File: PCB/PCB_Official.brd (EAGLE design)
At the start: 100 x 100 mm, 106 parts, among them IC1 MCP73871, J3 455-1750-1-ND, Q1 220mA/50V/3.5Ω, U1 TPS63070, U2 STM32F767ZIT6, U3 STM32L053C8T6, U4 TPS63070, U5 BATTERY-MANAGEMENT-TEMP_BQ274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

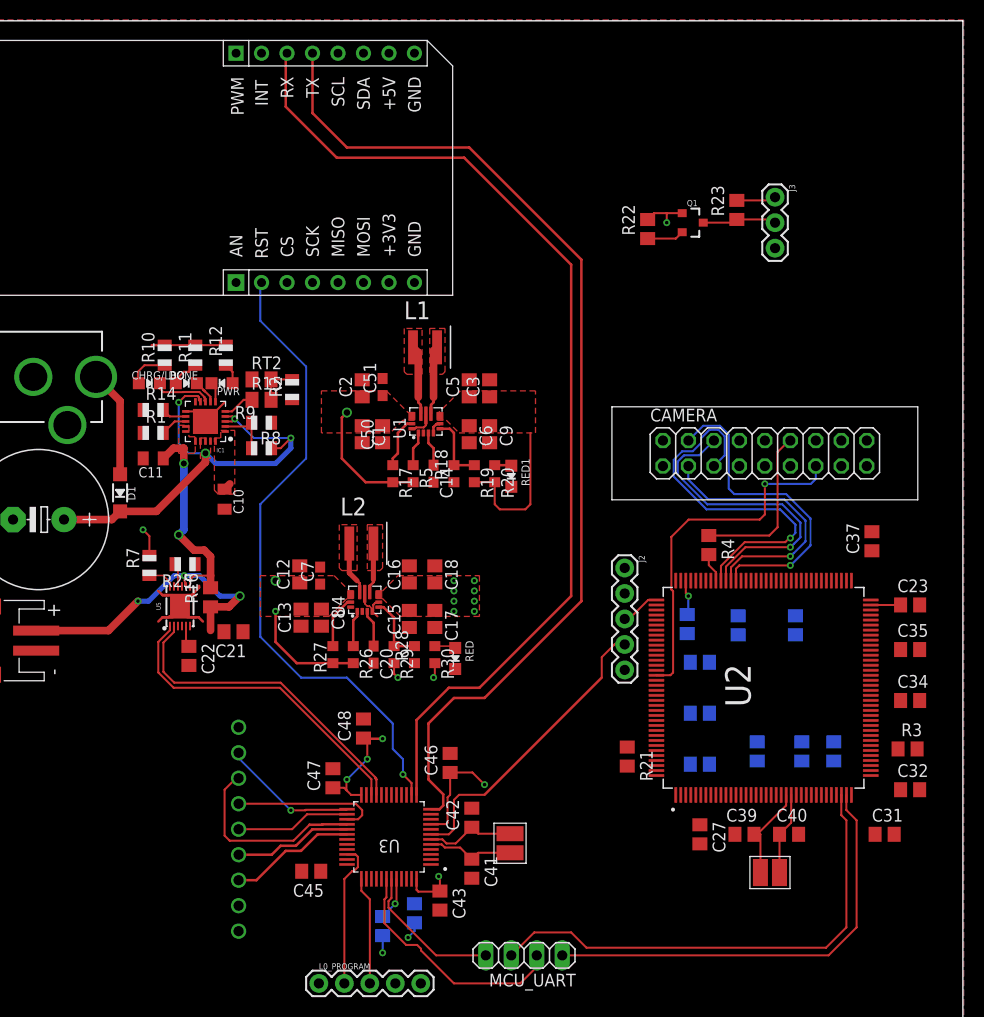
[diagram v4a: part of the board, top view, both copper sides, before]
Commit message: Added PCB pin assignments and routed camera connector.
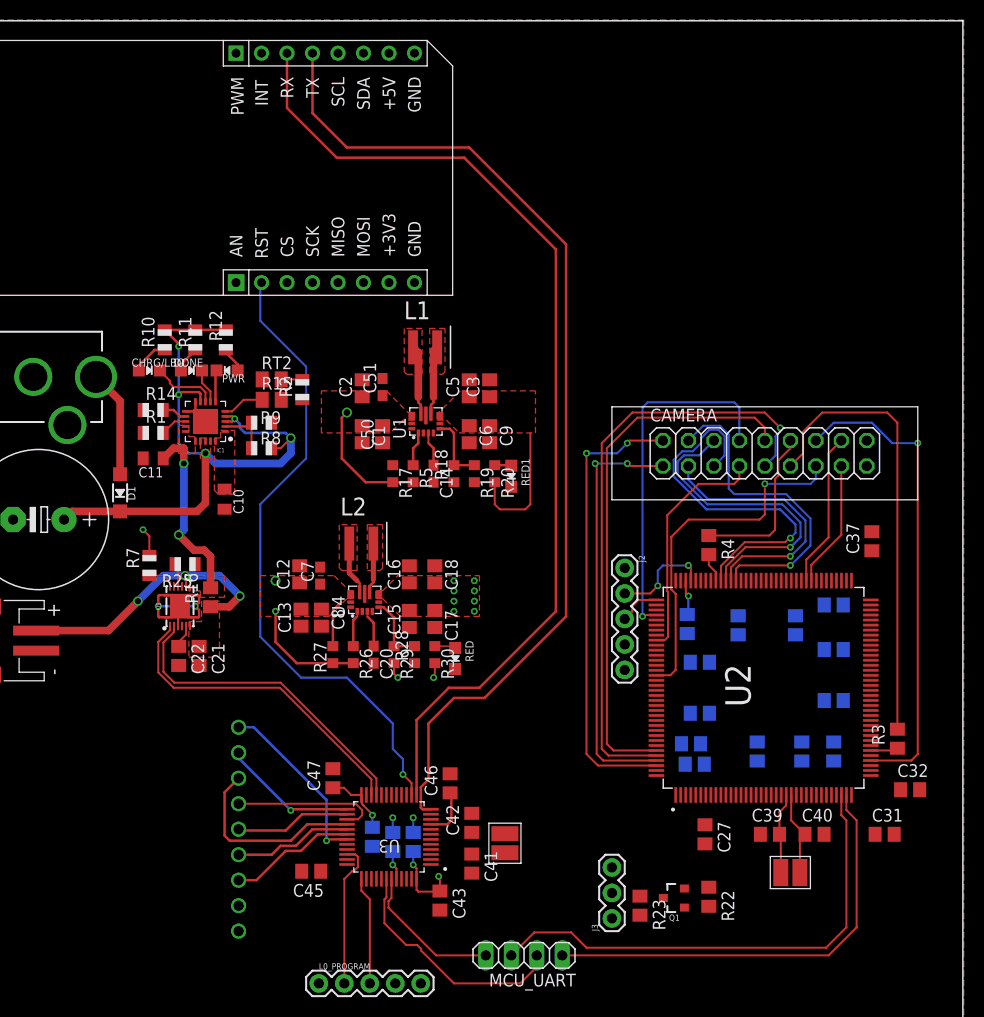
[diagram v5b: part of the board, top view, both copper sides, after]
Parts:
- moved J3 73.7 mm to (65.0, 10.5), turned to 90 degrees
- moved R23 70.0 mm to (67.8, 11.8), turned to 270 degrees
- moved Q1 67.3 mm to (71.2, 12.6), turned to 90 degrees
- moved R22 66.8 mm to (74.7, 12.7), turned to 270 degrees
- moved C48 10.8 mm to (41.1, 18.7), flipped to the bottom, turned to 270 degrees
- moved R24 8.44 mm to (43.2, 18.2), turned to 270 degrees
- moved C23 7.62 mm to (87.1, 41.8), flipped to the bottom
- moved C34 7.62 mm to (87.1, 32.3), flipped to the bottom
- moved C35 7.62 mm to (87.1, 37.3), flipped to the bottom
- moved C44 7.11 mm to (45.2, 18.2), turned to 90 degrees
- moved R21 6.48 mm to (72.9, 27.9), flipped to the bottom, turned to 180 degrees
- moved C21 4.19 mm to (23.9, 36.7), turned to 270 degrees
- moved C39 2.54 mm to (80.8, 18.9)
- moved C40 2.54 mm to (85.2, 18.9)
- moved C46 2.03 mm to (48.9, 24.0)
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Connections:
- removed net TIM3_CH2: Q1.2, R22.1, U2.135
- new net SERVO_PWM: Q1.2, R22.1, U2.18
- net CAM_PWDN: now also U2.142
- net CAM_RET: now also U2.141
- net LORA_RST: now also U3.31
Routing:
- net DCMI_D7: track 0.00 -> 60.3 mm, vias 0 -> 1
- net DCMI_D6: track 0.00 -> 53.4 mm
- net DCMI_HSYNC: track 0.00 -> 47.7 mm, vias 0 -> 1
- net CAM_PWDN: track 0.00 -> 45.6 mm, vias 0 -> 2
- net N$33: track 0.00 -> 45.1 mm
- net CAM_RET: track 0.00 -> 42.1 mm, vias 0 -> 2
- net DCMI_D4: track 0.00 -> 35.6 mm, vias 0 -> 1
- net MCU_RST: track 30.1 -> 0.00 mm
- net DCMI_D5: track 0.00 -> 23.4 mm
- net LORA_RST: track 0.00 -> 17.9 mm, vias 0 -> 1
- net CAM_SDA: track 0.00 -> 15.4 mm
- net CAM_SCL: track 0.00 -> 12.7 mm
- net +3V3: track 37.7 -> 25.7 mm, vias 17 -> 14
- net SYS_JTMS_SWDIO: track 0.00 -> 10.0 mm, vias 0 -> 2
- net VCC: track 56.1 -> 65.9 mm, vias 4 -> 5
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- added copper zone on layer 1, net N$22

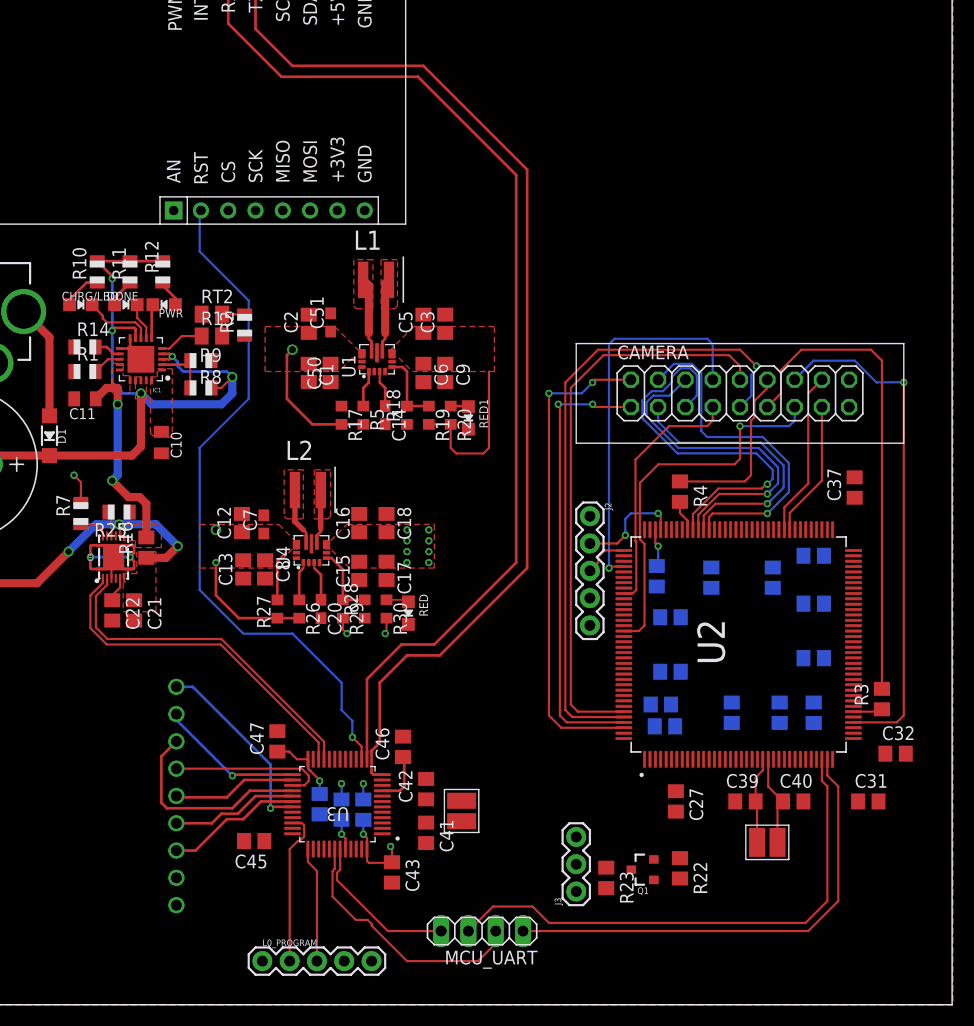
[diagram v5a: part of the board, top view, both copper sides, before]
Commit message: Corrected layout of 5V regulator, WIP for 3.3V regulator. Improved microcontroller layouts as well.
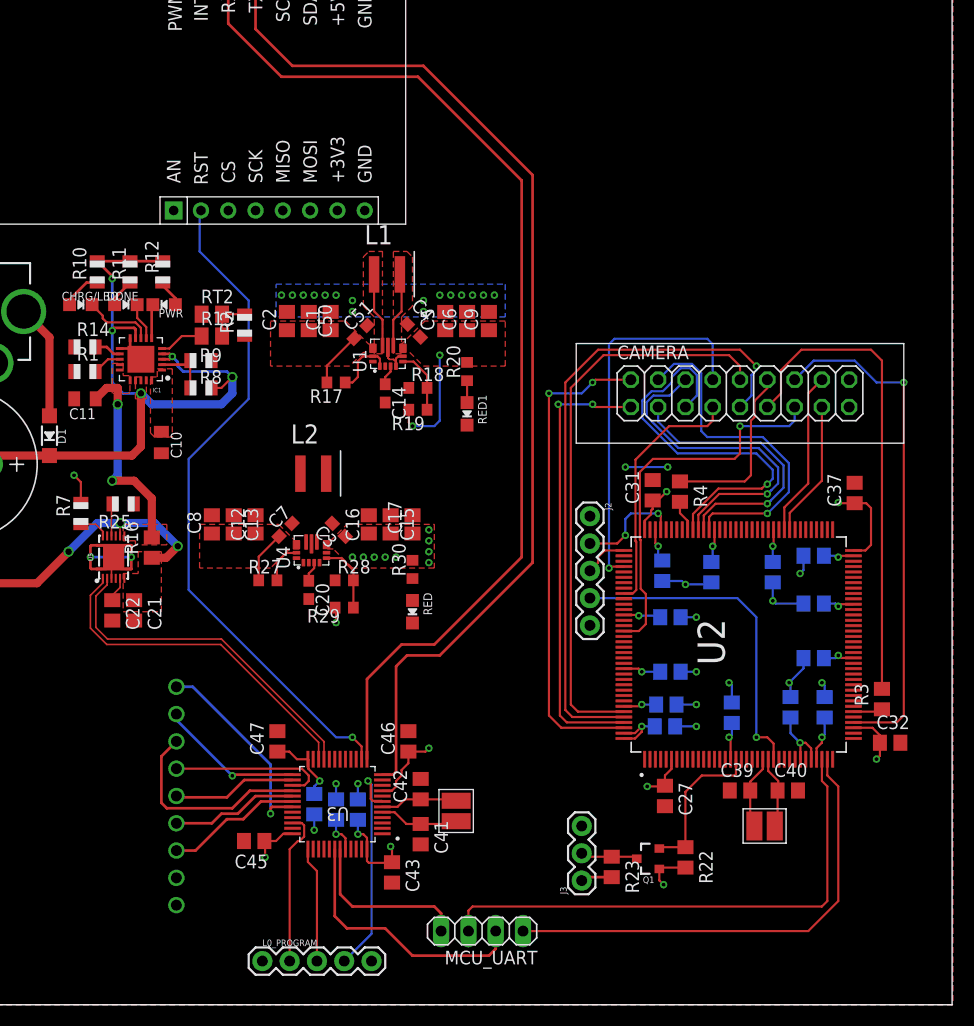
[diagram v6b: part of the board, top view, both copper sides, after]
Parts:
- removed C18: 10uF, adafruit:C0805
- removed R26, R5: 10k, rcl:R0603
- added C4: 10uF, rcl:C0603
- C13, C2: value 10uF -> 0.1uF
- C3: device adafruit:C0805 -> rcl:C0603
- C51, C7: value 0.1uF -> 10uF
- R18: value 68.1k -> 130k
- R19: value 365k -> 680k
- moved C31 35.2 mm to (72.1, 47.9), turned to 90 degrees
- moved C3 21.6 mm to (42.9, 44.2), turned to 135 degrees
- moved C8 6.49 mm to (31.1, 44.7), turned to 90 degrees
- moved C6 6.31 mm to (54.9, 63.6), turned to 90 degrees
- moved C9 6.31 mm to (56.9, 63.6), turned to 90 degrees
- moved C1 5.24 mm to (42.2, 63.6), turned to 90 degrees
- moved C50 5.24 mm to (40.1, 63.6), turned to 90 degrees
- moved C15 5.21 mm to (47.8, 44.7), turned to 90 degrees
- moved C17 4.95 mm to (49.8, 44.7), turned to 90 degrees
- moved R30 4.40 mm to (49.8, 40.5), turned to 90 degrees
- moved R20 4.34 mm to (54.9, 58.9), turned to 90 degrees
- moved C13 4.28 mm to (33.1, 44.7), turned to 90 degrees
- moved R28 3.28 mm to (43.4, 39.5), turned to 0 degrees
- moved R17 3.09 mm to (42.7, 57.9), turned to 180 degrees
- moved C51 2.93 mm to (45.0, 62.6), turned to 45 degrees
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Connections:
- removed net MCU_RST: J2.4, L0_PROGRAM.4, U2.25, U3.7
- removed net PS: R5.1, U1.P$1
- removed net PS1: R26.1, U4.P$1
- new net F7_RST: J2.4, U2.25
- new net L0_RST: L0_PROGRAM.4, U3.7
- net !EN: now also U1.P$1
- net !EN1: now also U4.P$1
- net +3V3: now also C3.1; no longer C18.1
- net +5V: now also C4.1; no longer C3.1
- net GND: now also C4.2; no longer C18.2
- net VOUT_CHARGER: no longer R26.2, R5.2
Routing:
- net +3V3: track 25.7 -> 97.0 mm, vias 14 -> 31
- net GND: track 20.2 -> 53.5 mm, vias 4 -> 33
- net F7_RST: track 0.00 -> 30.7 mm, vias 0 -> 1
- net L0_RST: track 0.00 -> 20.9 mm, vias 0 -> 1
- net VOUT_CHARGER: track 24.6 -> 10.0 mm, vias 3 -> 0
- net SERVO_PWM: track 0.00 -> 14.4 mm
- net N$31: track 0.00 -> 7.43 mm
- net N$30: track 0.00 -> 7.21 mm
- net !EN: track 0.00 -> 5.90 mm
- net N$29: track 0.00 -> 5.33 mm
- net N$7: track 5.27 -> 0.00 mm
- net N$8: track 4.98 -> 0.00 mm
- net PS: track 3.42 -> 0.00 mm
- net PS1: track 3.13 -> 0.00 mm
- net N$23: track 0.00 -> 3.07 mm, vias 0 -> 1
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- added copper zone on layer 16, net GND
- removed copper zone on layer 1, net N$7
- removed copper zone on layer 1, net N$8

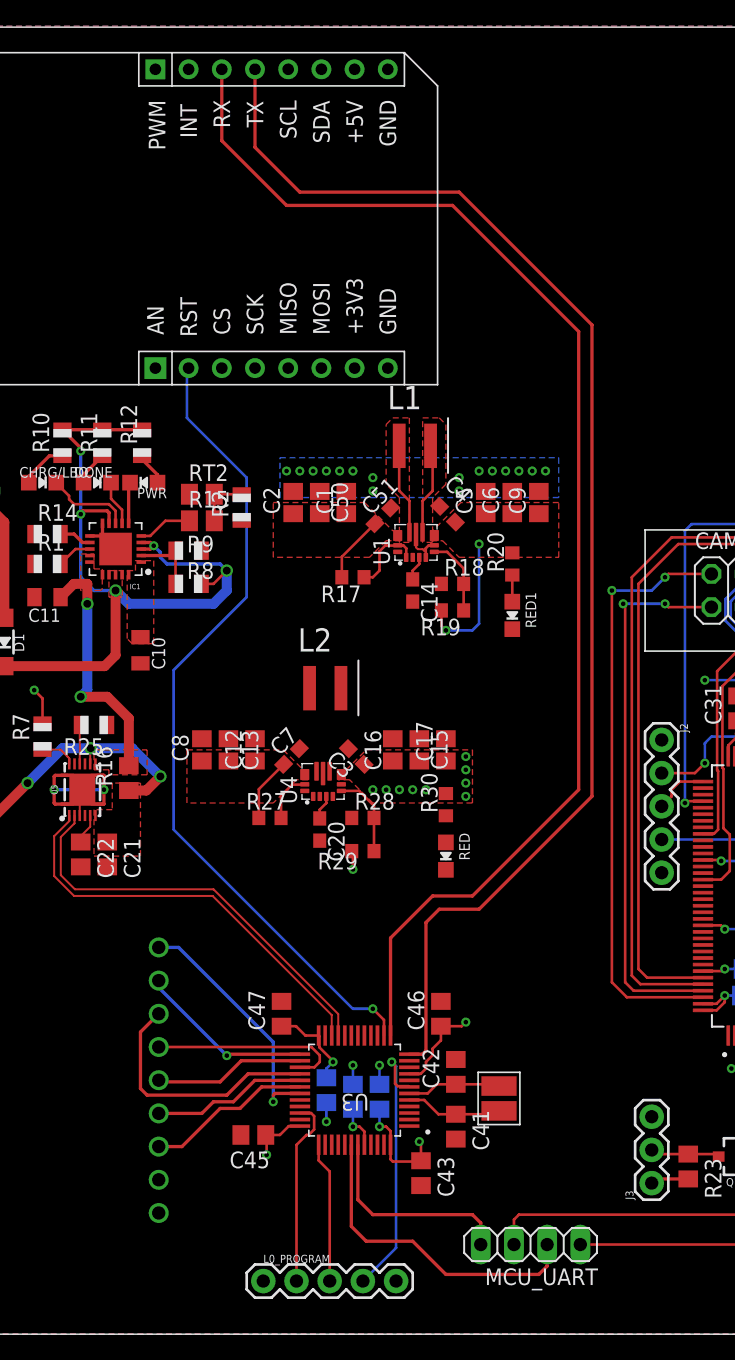
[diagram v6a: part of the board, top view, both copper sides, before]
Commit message: Passing DRU, need to fix silkscreen
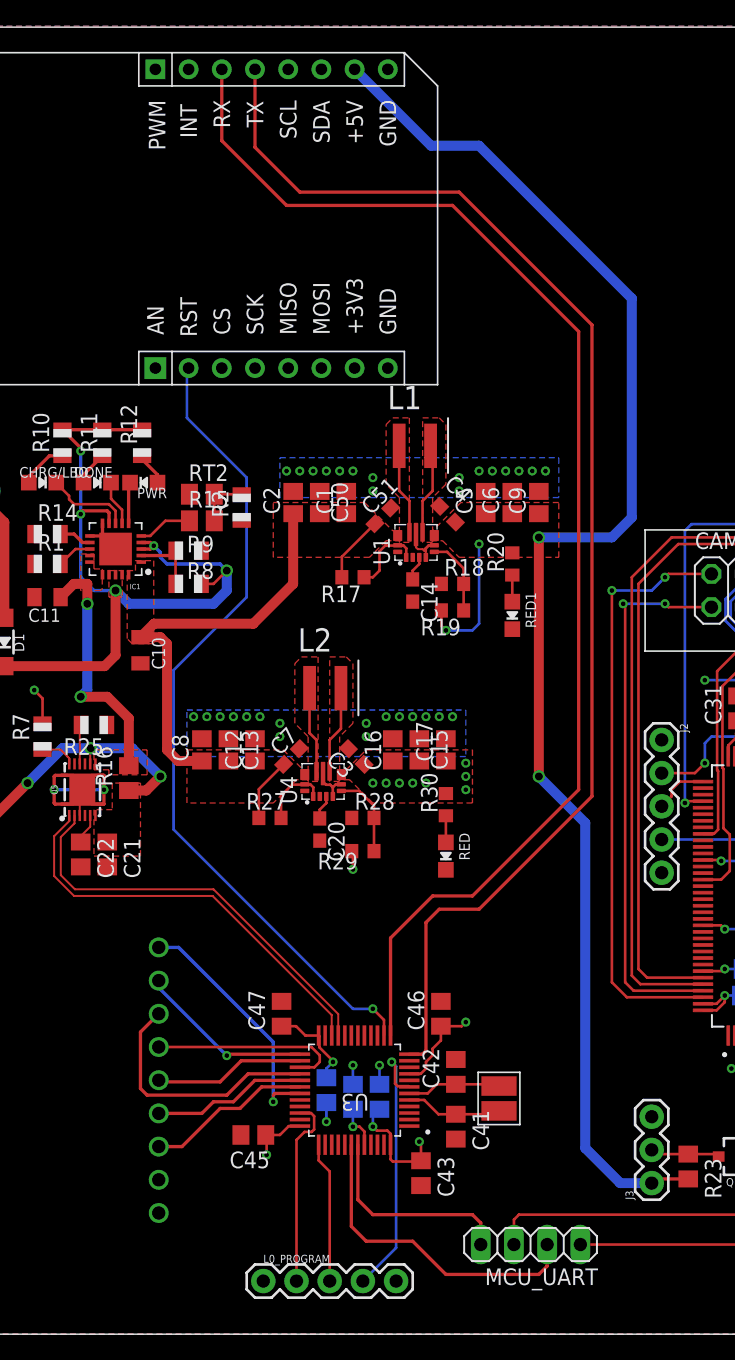
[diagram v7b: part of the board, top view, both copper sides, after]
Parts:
- BATT: value (none) -> BATT
- CN1: value (none) -> SOLAR
- J2: value (none) -> F7_PRGM
- L0_PROGRAM: value (none) -> L0_PRGM
- MCU_UART: value (none) -> MCU_UART
- R28: value 68.1k -> 150k
- R29: value 213k -> 470k
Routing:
- net +5V: track 13.4 -> 120.8 mm, vias 2 -> 4
- net VOUT_CHARGER: track 10.0 -> 42.2 mm
- net N$8: track 0.00 -> 6.72 mm
- net N$7: track 0.00 -> 6.58 mm
- net GND: track 53.5 -> 57.4 mm, vias 33 -> 49
- net N$20: track 0.00 -> 2.04 mm
- net !EN1: track 3.87 -> 5.33 mm
- net +3V3: track 97.0 -> 97.6 mm, vias 31 -> 30
- added copper zone on layer 1, net N$7
- added copper zone on layer 1, net N$8

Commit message: Submitted PCB for production.
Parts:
- added F7_LED1, F7_LED2, F7_LED3, L0_LED1, L0_LED2: ORANGE, microbuilder:CHIPLED_0805_NOOUTLINE
- added R13, R26, R31, R5, R6: 10k, rcl:R0805
- added R32, R33: (no value), rcl:R0805
- moved U$1 8.89 mm to (58.0, 72.6)
- moved L2 0.51 mm to (38.4, 48.1)
- moved R27 0.51 mm to (36.3, 39.0)
- renumbered CHRG/LBO to CHRG, CN1 to SOLAR, RED to 3.3V, RED1 to 5V
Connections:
- new net F7_LED1: R5.2, U2.58
- new net F7_LED2: R6.2, U2.56
- new net F7_LED3: R13.2, U2.54
- new net L0_LED1: R26.2, U3.20
- new net L0_LED2: R31.2, U3.18
- new net N$35: F7_LED2.A, R6.1
- new net N$36: F7_LED3.A, R13.1
- new net N$37: F7_LED1.A, R5.1
- new net N$38: L0_LED2.A, R31.1
- new net N$40: L0_LED1.A, R26.1
- net +3V3: now also R32.2, R33.2
- net BAT_SCL: now also R33.1
- net BAT_SDA: now also R32.1
- net GND: now also F7_LED1.C, F7_LED2.C, F7_LED3.C, L0_LED1.C, L0_LED2.C
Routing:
- net F7_LED1: track 0.00 -> 14.2 mm, vias 0 -> 2
- net RX_GSM: track 100.4 -> 89.3 mm
- net TX_GSM: track 101.3 -> 90.5 mm
- net F7_LED2: track 0.00 -> 9.66 mm, vias 0 -> 2
- net F7_LED3: track 0.00 -> 8.64 mm, vias 0 -> 2
- net +5V: track 120.8 -> 115.0 mm
- net L0_LED1: track 0.00 -> 5.23 mm
- net L0_LED2: track 0.00 -> 4.81 mm
- net BAT_SDA: track 32.3 -> 35.9 mm
- net N$40: track 0.00 -> 2.83 mm
- net N$38: track 0.00 -> 2.62 mm
- net +3V3: track 97.6 -> 100.0 mm, vias 30 -> 32
- net N$37: track 0.00 -> 2.07 mm
- net N$35: track 0.00 -> 2.07 mm
- net N$36: track 0.00 -> 2.07 mm
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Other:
- board text added: "3V3"
- board text added: "Badri Baskaran"
- board text added: "CLK"
- board text added: "DIO"
- board text added: "ECE 477 Group 11"
- board text added: "F7_RX"
- board text added: "F7_TX"
- board text added: "GND"
- board text added: "Hazwan Zainudin"
- board text added: "L0_RX"
- board text added: "L0_TX"
- board text added: "Luke Kok"
- board text added: "RST"
- board text added: "Sreyas Mirthipati"
